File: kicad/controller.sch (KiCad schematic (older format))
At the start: 7 parts, among them U2 74LVC1G125, U3 NST175

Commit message: BOM ist nun fast fertig
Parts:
- R6: value 4k7 -> 10k; PriceEUR (none) -> 0.01
- R7, R8: value 4k7 -> 3k3; PriceEUR (none) -> 0.01
- U3: Notes (none) -> digital temperature sensor, +/-0.5°C, I2C; PriceEUR (none) -> 0.096; PriceForQty (none) -> 10; Weblink (none) -> https://lcsc.com/product-detail/Temperature-Sensors_NOVOSEN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
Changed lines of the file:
@@
 P 7000 3800
 F 0 "R7" H 7070 3846 50  0000 L CNN
-F 1 "4k7" H 7070 3755 50  0000 L CNN
+F 1 "3k3" H 7070 3755 50  0000 L CNN
 F 2 "Resistor_SMD:R_1206_3216Metric" V 6930 3800 50  0001 C CNN
 F 3 "~" H 7000 3800 50  0001 C CNN
+F 4 "0.01" H 7000 3800 50  0001 C CNN "PriceEUR"
 	1    7000 3800
 	1    0    0    -1
@@
 P 7300 3800
 F 0 "R8" H 7370 3846 50  0000 L CNN
-F 1 "4k7" H 7370 3755 50  0000 L CNN
+F 1 "3k3" H 7370 3755 50  0000 L CNN
 F 2 "Resistor_SMD:R_1206_3216Metric" V 7230 3800 50  0001 C CNN
 F 3 "~" H 7300 3800 50  0001 C CNN
+F 4 "0.01" H 7300 3800 50  0001 C CNN "PriceEUR"
 	1    7300 3800
 	1    0    0    -1
@@
 F 4 "LCSC" H 9450 4150 50  0001 C CNN "Distributor"
 F 5 "C967852" H 9450 4150 50  0001 C CNN "DistOrderNr"
+F 6 "digital temperature sensor, +/-0.5°C, I2C" H 9450 4150 50  0001 C CNN "Notes"
+F 7 "0.096" H 9450 4150 50  0001 C CNN "PriceEUR"
+F 8 "10" H 9450 4150 50  0001 C CNN "PriceForQty"
+F 9 "https://lcsc.com/product-detail/Temperature-Sensors_NOVOSENSE-NST175-QSPR_C967852.html" H 9450 4150 50  0001 C CNN "Weblink"
 	1    9450 4150
 	1    0    0    -1
@@
 P 2500 2300
 F 0 "R6" H 2570 2346 50  0000 L CNN
-F 1 "4k7" H 2570 2255 50  0000 L CNN
+F 1 "10k" H 2570 2255 50  0000 L CNN
 F 2 "Resistor_SMD:R_1206_3216Metric" V 2430 2300 50  0001 C CNN
 F 3 "~" H 2500 2300 50  0001 C CNN
+F 4 "0.01" H 2500 2300 50  0001 C CNN "PriceEUR"
 	1    2500 2300
 	1    0    0    -1

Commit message: BOM Fertig, 3D auch fast fertig. Ein paar Footrpints fehlen noch.
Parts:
- removed A1: Arduino_Nano_v3.x, Module:Arduino_Nano, symbol MCU_Module:Arduino_Nano_v3.x
- added C5: 100n, Capacitor_SMD:C_1206_3216Metric, symbol Device:C
- added D2: BAV99, Package_TO_SOT_SMD:SOT-23, symbol Diode:BAV99
- added R7: 10k, Resistor_SMD:R_1206_3216Metric, symbol Device:R
- R6: DistOrderNr (none) -> C118075; Distributor (none) -> LCSC
- R8: renamed from R7; DistOrderNr (none) -> C229599; Distributor (none) -> LCSC
- R9: renamed from R8; DistOrderNr (none) -> C229599; Distributor (none) -> LCSC
- U3: footprint Package_SO:SO-8_3.9x4.9mm_P1.27mm -> Package_SO:SOIC-8_3.9x4.9mm_P1.27mm
- renumbered C5 to C6
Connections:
- net labels added: Lötkolbenständer, VUSB
- net labels removed: ~RS232-Rx-Enable
- wire segments 61 -> 78
- no-connect marks 6 -> 5
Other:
- note added: "Kondensator \nwichtig für ESD-Schutz"
- note added: "Schutzwiderstand\ngegen 60V"

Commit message: kleinere Updates im Schaltplan
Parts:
- D2: symbol Diode:BAV99 -> jbc-miniregler-rescue:BAV99-Diode
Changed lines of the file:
@@
 Schutzwiderstand\ngegen 60V
 $Comp
-L Diode:BAV99 D?
+L jbc-miniregler-rescue:BAV99-Diode D?
 U 1 1 60B5DBF4
 P 2350 5100
@@
 $EndComp
 $Comp
-L Diode:BAV99 D?
+L jbc-miniregler-rescue:BAV99-Diode D?
 U 2 1 60B5F1E3
 P 2800 5100

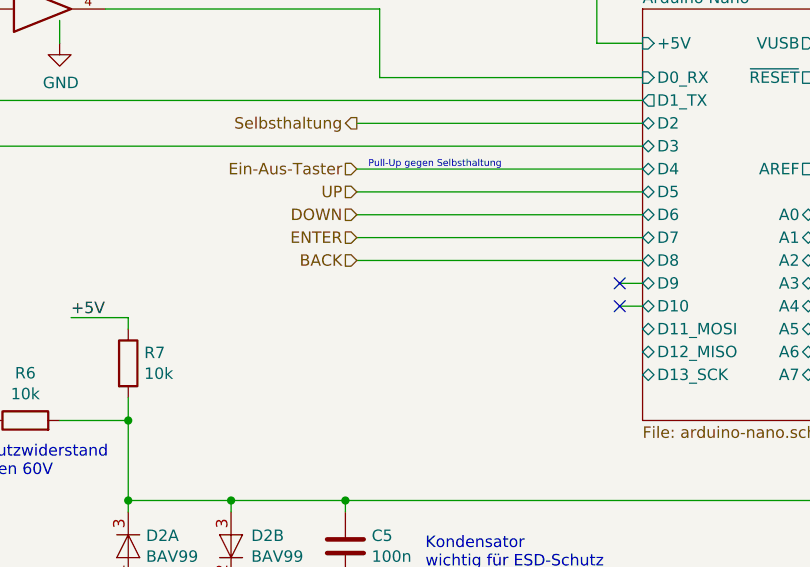
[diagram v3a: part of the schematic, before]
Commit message: um Option RS485 erweitert
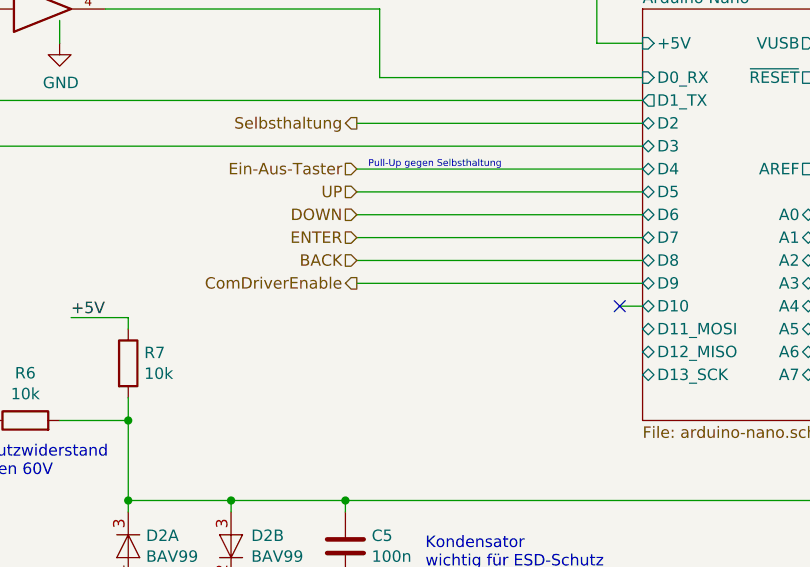
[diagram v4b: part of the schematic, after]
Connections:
- no-connect marks 5 -> 4
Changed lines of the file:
@@
 Kondensator \nwichtig für ESD-Schutz
-Wire Wire Line
-	4600 3950 4500 3950
-NoConn ~ 4500 3950
 Wire Wire Line
 	4500 4050 4600 4050
 NoConn ~ 4500 4050
+Text HLabel 3350 3950 0    50   Output ~ 0
+ComDriverEnable
+Wire Wire Line
+	3350 3950 4600 3950
 $EndSCHEMATC

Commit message: OPV-Polaritätsoption, Zusatzfilter und Strombegrenzung
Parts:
- added R? (x2): 1k, Resistor_SMD:R_1206_3216Metric, symbol Device:R
- added U?: TL431DBZ, Package_TO_SOT_SMD:SOT-23, symbol Reference_Voltage:TL431DBZ
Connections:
- wire segments 78 -> 90
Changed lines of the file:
@@
 Wire Wire Line
 	3350 3950 4600 3950
+$Comp
+L Reference_Voltage:TL431DBZ U?
+U 1 1 60B78F6B
+P 6950 2800
+F 0 "U?" V 6996 2730 50  0000 R CNN
+F 1 "TL431DBZ" V 6905 2730 50  0000 R CNN
+F 2 "Package_TO_SOT_SMD:SOT-23" H 6950 2650 50  0001 C CIN
+F 3 "http://www.ti.com/lit/ds/symlink/tl431.pdf" H 6950 2800 50  0001 C CIN
+	1    6950 2800
+	0    -1   -1   0
+$EndComp
+$Comp
+L power:GND #PWR?
+U 1 1 60B79FC6
+P 6950 2900
+F 0 "#PWR?" H 6950 2650 50  0001 C CNN
+F 1 "GND" H 6955 2727 50  0000 C CNN
+F 2 "" H 6950 2900 50  0001 C CNN
+F 3 "" H 6950 2900 50  0001 C CNN
+	1    6950 2900
+	1    0    0    -1
+$EndComp
+Wire Wire Line
+	6850 2800 6850 2600
+Wire Wire Line
+	6850 2600 6950 2600
+Wire Wire Line
+	6950 2600 6950 2700
+$Comp
+L Device:R R?
+U 1 1 60B8161C
+P 6950 2250
+AR Path="/608DBC3C/60B8161C" Ref="R?"  Part="1"
+AR Path="/60B8161C" Ref="R?"  Part="1"
+F 0 "R?" H 7020 2296 50  0000 L CNN
+F 1 "1k" H 7020 2205 50  0000 L CNN
+F 2 "Resistor_SMD:R_1206_3216Metric" V 6880 2250 50  0001 C CNN
+F 3 "~" H 6950 2250 50  0001 C CNN
+F 4 "0.0042" H 6950 2250 50  0001 C CNN "PriceEUR"
+F 5 "C104601" H 6950 2250 50  0001 C CNN "DistOrderNr"
+F 6 "LCSC" H 6950 2250 50  0001 C CNN "Distributor"
+F 7 "RTT03101JTP" H 6950 2250 50  0001 C CNN "ManPartNr"
+F 8 "RALEC" H 6950 2250 50  0001 C CNN "Manufacturer"
+F 9 "1kΩ ±5% 0.25W ±100ppm/℃ 1206 Chip Resistor" H 6950 2250 50  0001 C CNN "Notes"
+F 10 "50" H 6950 2250 50  0001 C CNN "PriceForQty"
+	1    6950 2250
+	1    0    0    -1
+$EndComp
+$Comp
+L Device:R R?
+U 1 1 60B83876
+P 7200 2250
+AR Path="/608DBC3C/60B83876" Ref="R?"  Part="1"
+AR Path="/60B83876" Ref="R?"  Part="1"
+F 0 "R?" H 7270 2296 50  0000 L CNN
+F 1 "1k" H 7270 2205 50  0000 L CNN
+F 2 "Resistor_SMD:R_1206_3216Metric" V 7130 2250 50  0001 C CNN
+F 3 "~" H 7200 2250 50  0001 C CNN
+F 4 "0.0042" H 7200 2250 50  0001 C CNN "PriceEUR"
+F 5 "C104601" H 7200 2250 50  0001 C CNN "DistOrderNr"
+F 6 "LCSC" H 7200 2250 50  0001 C CNN "Distributor"
+F 7 "RTT03101JTP" H 7200 2250 50  0001 C CNN "ManPartNr"
+F 8 "RALEC" H 7200 2250 50  0001 C CNN "Manufacturer"
+F 9 "1kΩ ±5% 0.25W ±100ppm/℃ 1206 Chip Resistor" H 7200 2250 50  0001 C CNN "Notes"
+F 10 "50" H 7200 2250 50  0001 C CNN "PriceForQty"
+	1    7200 2250
+	1    0    0    -1
+$EndComp
+Wire Wire Line
+	6950 2600 6950 2400
+Connection ~ 6950 2600
+Wire Wire Line
+	6950 2600 7200 2600
+Wire Wire Line
+	7200 2600 7200 2400
+Wire Wire Line
+	6950 1950 7200 1950
+Wire Wire Line
+	7200 1950 7200 2100
+Wire Wire Line
+	6950 1950 6950 2100
+Wire Wire Line
+	6850 2600 6550 2600
+Wire Wire Line
+	5550 3050 5550 3450
+Wire Wire Line
+	5550 3450 5350 3450
+Connection ~ 6850 2600
 $EndSCHEMATC

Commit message: Neu: Spannungsreferenz TL431, Laout Fertig, TODO: Labels
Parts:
- removed U?: TL431DBZ, Package_TO_SOT_SMD:SOT-23, symbol Reference_Voltage:TL431DBZ
- added U12: TL431, Package_TO_SOT_SMD:SOT-23, symbol htl_ics:TL431
- gave numbers to parts that had none: 2
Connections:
- wire segments 90 -> 91
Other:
- note added: "Vref 2.5V"
- moved on the sheet: R63, R64
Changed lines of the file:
@@
 	3350 3950 4600 3950
 $Comp
-L Reference_Voltage:TL431DBZ U?
-U 1 1 60B78F6B
-P 6950 2800
-F 0 "U?" V 6996 2730 50  0000 R CNN
-F 1 "TL431DBZ" V 6905 2730 50  0000 R CNN
-F 2 "Package_TO_SOT_SMD:SOT-23" H 6950 2650 50  0001 C CIN
-F 3 "http://www.ti.com/lit/ds/symlink/tl431.pdf" H 6950 2800 50  0001 C CIN
-	1    6950 2800
-	0    -1   -1   0
-$EndComp
-$Comp
-L power:GND #PWR?
+L power:GND #PWR0111
 U 1 1 60B79FC6
-P 6950 2900
-F 0 "#PWR?" H 6950 2650 50  0001 C CNN
-F 1 "GND" H 6955 2727 50  0000 C CNN
-F 2 "" H 6950 2900 50  0001 C CNN
-F 3 "" H 6950 2900 50  0001 C CNN
-	1    6950 2900
+P 6350 3400
+F 0 "#PWR0111" H 6350 3150 50  0001 C CNN
+F 1 "GND" H 6355 3227 50  0000 C CNN
+F 2 "" H 6350 3400 50  0001 C CNN
+F 3 "" H 6350 3400 50  0001 C CNN
+	1    6350 3400
 	1    0    0    -1
 $EndComp
 Wire Wire Line
-	6850 2800 6850 2600
+	6200 3000 6350 3000
 Wire Wire Line
-	6850 2600 6950 2600
-Wire Wire Line
-	6950 2600 6950 2700
+	6350 3000 6350 3100
 $Comp
-L Device:R R?
+L Device:R R63
 U 1 1 60B8161C
-P 6950 2250
-AR Path="/608DBC3C/60B8161C" Ref="R?"  Part="1"
+P 6350 2650
+AR Path="/608DBC3C/60B8161C" Ref="R63"  Part="1"
 AR Path="/60B8161C" Ref="R?"  Part="1"
-F 0 "R?" H 7020 2296 50  0000 L CNN
-F 1 "1k" H 7020 2205 50  0000 L CNN
-F 2 "Resistor_SMD:R_1206_3216Metric" V 6880 2250 50  0001 C CNN
-F 3 "~" H 6950 2250 50  0001 C CNN
-F 4 "0.0042" H 6950 2250 50  0001 C CNN "PriceEUR"
-F 5 "C104601" H 6950 2250 50  0001 C CNN "DistOrderNr"
-F 6 "LCSC" H 6950 2250 50  0001 C CNN "Distributor"
-F 7 "RTT03101JTP" H 6950 2250 50  0001 C CNN "ManPartNr"
-F 8 "RALEC" H 6950 2250 50  0001 C CNN "Manufacturer"
-F 9 "1kΩ ±5% 0.25W ±100ppm/℃ 1206 Chip Resistor" H 6950 2250 50  0001 C CNN "Notes"
-F 10 "50" H 6950 2250 50  0001 C CNN "PriceForQty"
-	1    6950 2250
+F 0 "R63" H 6281 2696 50  0000 R CNN
+F 1 "1k" H 6281 2605 50  0000 R CNN
+F 2 "Resistor_SMD:R_1206_3216Metric" V 6280 2650 50  0001 C CNN
+F 3 "~" H 6350 2650 50  0001 C CNN
+F 4 "0.0042" H 6350 2650 50  0001 C CNN "PriceEUR"
+F 5 "C104601" H 6350 2650 50  0001 C CNN "DistOrderNr"
+F 6 "LCSC" H 6350 2650 50  0001 C CNN "Distributor"
+F 7 "RTT03101JTP" H 6350 2650 50  0001 C CNN "ManPartNr"
+F 8 "RALEC" H 6350 2650 50  0001 C CNN "Manufacturer"
+F 9 "1kΩ ±5% 0.25W ±100ppm/℃ 1206 Chip Resistor" H 6350 2650 50  0001 C CNN "Notes"
+F 10 "50" H 6350 2650 50  0001 C CNN "PriceForQty"
+	1    6350 2650
 	1    0    0    -1
 $EndComp
 $Comp
-L Device:R R?
+L Device:R R64
 U 1 1 60B83876
-P 7200 2250
-AR Path="/608DBC3C/60B83876" Ref="R?"  Part="1"
+P 6600 2650
+AR Path="/608DBC3C/60B83876" Ref="R64"  Part="1"
 AR Path="/60B83876" Ref="R?"  Part="1"
-F 0 "R?" H 7270 2296 50  0000 L CNN
-F 1 "1k" H 7270 2205 50  0000 L CNN
-F 2 "Resistor_SMD:R_1206_3216Metric" V 7130 2250 50  0001 C CNN
-F 3 "~" H 7200 2250 50  0001 C CNN
-F 4 "0.0042" H 7200 2250 50  0001 C CNN "PriceEUR"
-F 5 "C104601" H 7200 2250 50  0001 C CNN "DistOrderNr"
-F 6 "LCSC" H 7200 2250 50  0001 C CNN "Distributor"
-F 7 "RTT03101JTP" H 7200 2250 50  0001 C CNN "ManPartNr"
-F 8 "RALEC" H 7200 2250 50  0001 C CNN "Manufacturer"
-F 9 "1kΩ ±5% 0.25W ±100ppm/℃ 1206 Chip Resistor" H 7200 2250 50  0001 C CNN "Notes"
-F 10 "50" H 7200 2250 50  0001 C CNN "PriceForQty"
-	1    7200 2250
+F 0 "R64" H 6670 2696 50  0000 L CNN
+F 1 "1k" H 6670 2605 50  0000 L CNN
+F 2 "Resistor_SMD:R_1206_3216Metric" V 6530 2650 50  0001 C CNN
+F 3 "~" H 6600 2650 50  0001 C CNN
+F 4 "0.0042" H 6600 2650 50  0001 C CNN "PriceEUR"
+F 5 "C104601" H 6600 2650 50  0001 C CNN "DistOrderNr"
+F 6 "LCSC" H 6600 2650 50  0001 C CNN "Distributor"
+F 7 "RTT03101JTP" H 6600 2650 50  0001 C CNN "ManPartNr"
+F 8 "RALEC" H 6600 2650 50  0001 C CNN "Manufacturer"
+F 9 "1kΩ ±5% 0.25W ±100ppm/℃ 1206 Chip Resistor" H 6600 2650 50  0001 C CNN "Notes"
+F 10 "50" H 6600 2650 50  0001 C CNN "PriceForQty"
+	1    6600 2650
 	1    0    0    -1
 $EndComp
 Wire Wire Line
-	6950 2600 6950 2400
-Connection ~ 6950 2600
+	6350 3000 6350 2800
+Connection ~ 6350 3000
 Wire Wire Line
-	6950 2600 7200 2600
+	6350 3000 6600 3000
 Wire Wire Line
-	7200 2600 7200 2400
+	6600 3000 6600 2800
 Wire Wire Line
-	6950 1950 7200 1950
+	6350 2350 6600 2350
 Wire Wire Line
-	7200 1950 7200 2100
+	6600 2350 6600 2500
 Wire Wire Line
-	6950 1950 6950 2100
-Wire Wire Line
-	6850 2600 6550 2600
-Wire Wire Line
-	5550 3050 5550 3450
+	6350 2350 6350 2500
 Wire Wire Line
 	5550 3450 5350 3450
-Connection ~ 6850 2600
+Connection ~ 6200 3000
+Wire Wire Line
+	5550 3000 6200 3000
+Wire Wire Line
+	5550 3000 5550 3450
+Text Label 6050 2350 0    50   ~ 0
++5V
+Wire Wire Line
+	6050 2350 6350 2350
+Connection ~ 6350 2350
+Wire Wire Line
+	6200 3000 6200 3250
+Text Notes 5750 3000 0    50   ~ 0
+Vref 2.5V
+$Comp
+L htl_ics:TL431 U12
+U 1 1 60B6FC4B
+P 6350 3250
+F 0 "U12" H 6438 3296 50  0000 L CNN
+F 1 "TL431" H 6438 3205 50  0000 L CNN
+F 2 "Package_TO_SOT_SMD:SOT-23" H 6350 3100 50  0001 C CIN
+F 3 "https://datasheet.lcsc.com/lcsc/1809211429_Guangdong-Hottech-TL431_C181103.pdf" H 6350 3250 50  0001 C CIN
+F 4 "LCSC" H 6350 3250 50  0001 C CNN "Distributor"
+F 5 "C181103" H 6350 3250 50  0001 C CNN "DistOrderNr"
+F 6 "0.021" H 6350 3250 50  0001 C CNN "PriceEUR"
+F 7 "200" H 6350 3250 50  0001 C CNN "PriceForQty"
+F 8 "https://lcsc.com/product-detail/Voltage-References_Guangdong-Hottech-TL431_C181103.html" H 6350 3250 50  0001 C CNN "Weblink"
+F 9 "2.5V, +/-0.5%, +/-50ppm/K, SOT-23, Ref-Kath-Ano" H 6350 3250 50  0001 C CNN "Notes"
+	1    6350 3250
+	1    0    0    -1
+$EndComp
 $EndSCHEMATC

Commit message: wip, bugfixes für v21.0.1
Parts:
- R6, R7: Notes (none) -> 10kΩ ±5% 0.25W ±100ppm/℃ 3216 Chip Resistor
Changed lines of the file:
@@
 Sheet 2 10
 Title "HTL Lötregler Mini"
-Date "2021-06-01"
-Rev "21.0.0"
+Date "2021-09-22"
+Rev "21.0.1-dev"
 Comp "HTL Steyr"
 Comment1 "Prof. Karl Zeilhofer et al."
@@
 F 5 "C118075" H 1900 4550 50  0001 C CNN "DistOrderNr"
 F 6 "LCSC" H 1900 4550 50  0001 C CNN "Distributor"
+F 7 "10kΩ ±5% 0.25W ±100ppm/℃ 3216 Chip Resistor" H 1900 4550 50  0001 C CNN "Notes"
 	1    1900 4550
 	0    -1   -1   0
@@
 F 5 "C118075" H 2350 4300 50  0001 C CNN "DistOrderNr"
 F 6 "LCSC" H 2350 4300 50  0001 C CNN "Distributor"
+F 7 "10kΩ ±5% 0.25W ±100ppm/℃ 3216 Chip Resistor" H 2350 4300 50  0001 C CNN "Notes"
 	1    2350 4300
 	1    0    0    -1
